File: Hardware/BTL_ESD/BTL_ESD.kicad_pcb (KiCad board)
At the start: 2 copper layers, 73.4 x 95.8 mm, 145 parts, among them J1 DC-005-5A-2.0, J2 BOOT, J3 Load Program, J4 Socket_TFT_1, J5 Socket_TFT_2, J6 USB_B_Micro, J7 220VAC, K1 SRD-05VDC-SL-C, Q1 MMBT2222A, Q2 MMBT2222A, Q3 MMBT2222A, Q4 MMBT2222A, SW1 MS-22D18G2ROHS, SW2 RESET, SW3 ENABLE, SW4 FLASH, U1 ICL7662CBA-T, U2 AMS1117-3.3, U3 TPS54331D, U4 STM32F103RCTx, U5 ESP32-WROOM-32E__4MB_HIGH_TEM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, U6 MCP6002-E_SN, U7 INA128UA, U8 CH340C, U9 PC817, Y1 8MHz, Y2 32.768KHz

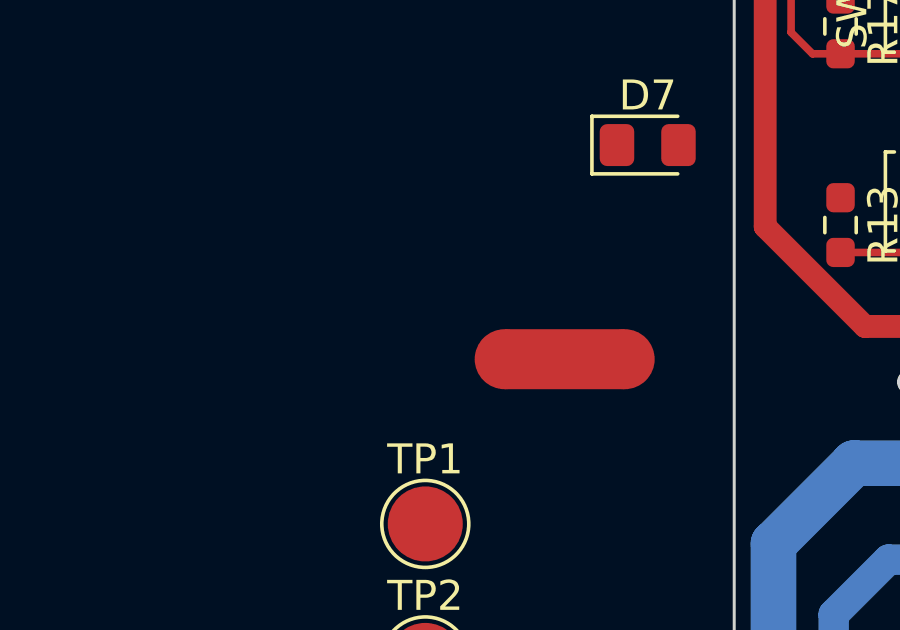
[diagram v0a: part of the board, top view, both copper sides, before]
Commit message: fix:STM32: update structure folder Libs
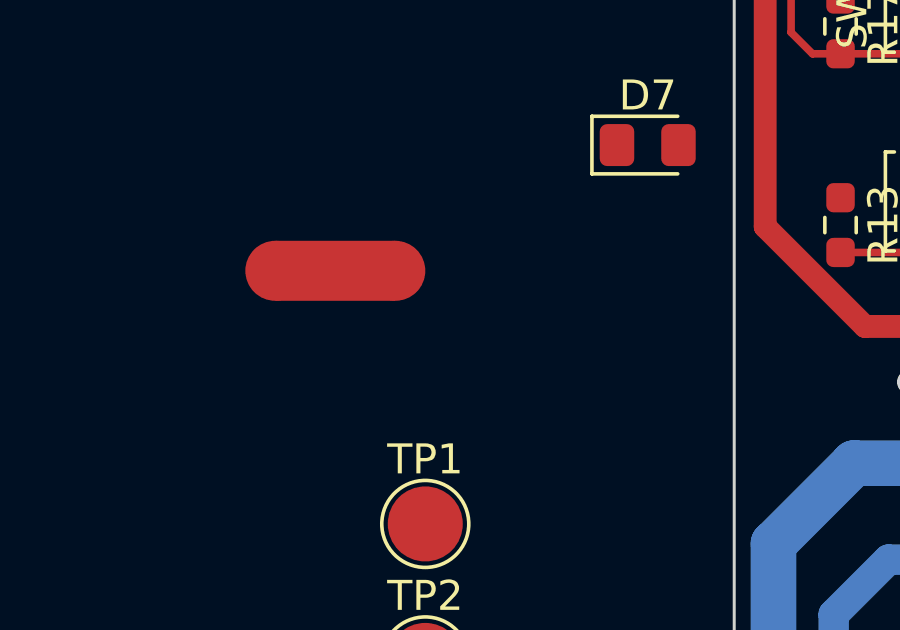
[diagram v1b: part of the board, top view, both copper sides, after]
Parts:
- moved NT1 8.19 mm to (140.0, 88.5)
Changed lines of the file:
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@@
   )
   (footprint "NetTie:NetTie-2_SMD_Pad2.0mm" (layer "F.Cu")
-    (at 147.6248 91.4146)
+    (at 139.9794 88.4682)
     (descr "Net tie, 2 pin, 2.0mm square SMD pads")
     (tags "net tie")

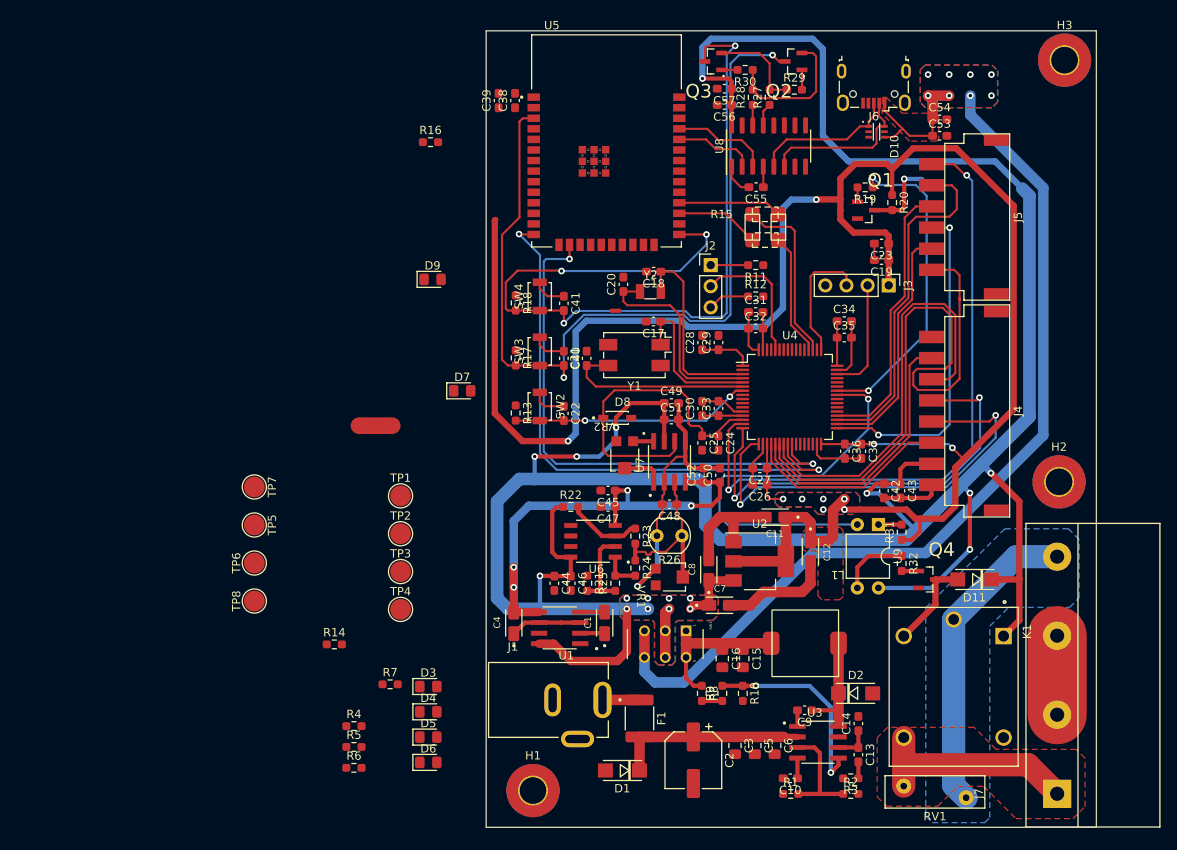
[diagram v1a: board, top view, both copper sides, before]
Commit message: hardware:update pcb track power
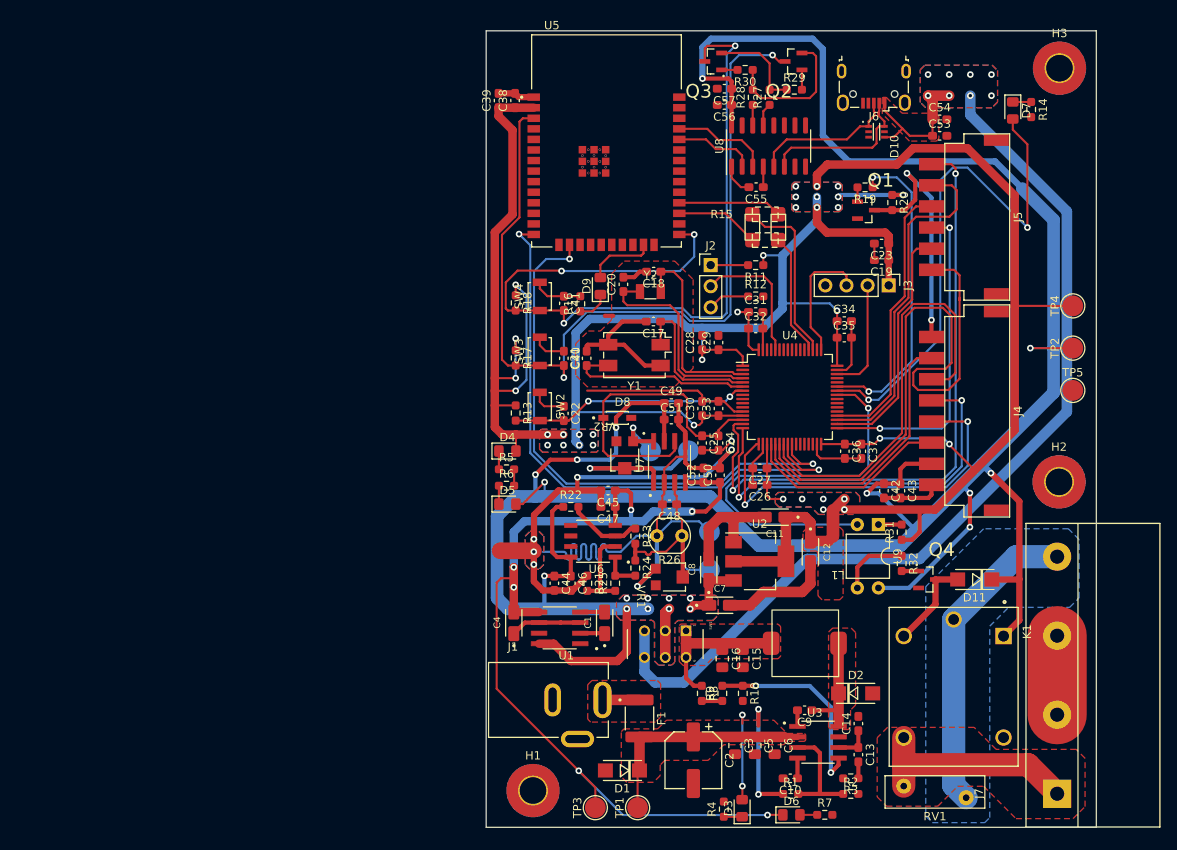
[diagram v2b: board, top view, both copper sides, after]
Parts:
- added TP5: GND, TestPoint:TestPoint_Pad_D2.5mm, F.Cu at (223.8, 84.2)
- TP6: renamed from TP5; moved to B.Cu
- TP7: renamed from TP6; moved to B.Cu
- TP8: renamed from TP7; moved to B.Cu
- TP9: renamed from TP8; moved to B.Cu
- moved R14 105.6 mm to (218.8, 50.5), turned to -90 degrees
- moved TP4 88.7 mm to (223.8, 74.1), turned to 90 degrees
- moved TP2 83.8 mm to (223.8, 79.1), turned to 90 degrees
- moved D7 74.3 mm to (216.6, 50.6), turned to -90 degrees
- moved TP6 55.0 mm to (180.1, 105.8), turned to 90 degrees
- moved TP7 54.8 mm to (180.1, 101.2)
- moved R7 54.6 mm to (194.0, 135.3)
- moved TP8 52.4 mm to (177.6, 91.5), turned to 180 degrees
- moved TP9 50.9 mm to (173.0, 91.5), turned to 180 degrees
- moved TP1 47.1 mm to (171.5, 134.4), turned to 90 degrees
- moved R4 45.6 mm to (181.8, 134.6), turned to 90 degrees
- moved D6 44.1 mm to (190.0, 135.3)
- moved D3 40.5 mm to (184.0, 134.5), turned to 90 degrees
- moved R6 38.6 mm to (155.7, 95.7)
- moved R5 38.1 mm to (155.7, 93.7)
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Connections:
- R13 pad 1: +3.3V -> +3V3
- U4 pad 2: /STM32/LED_TEST -> unconnected-(U4-PC13-Pad2)
- U4 pad 42: TFT_BL -> /STM32/LED_TEST
- U4 pad 43: unconnected-(U4-PA10-Pad43) -> TFT_BL
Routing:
- net +3V3: track 270.4 -> 370.1 mm, vias 10 -> 35
- net GNDA: track 33.6 -> 122.3 mm, vias 1 -> 6
- net /STM32/LED_TEST: track 0.00 -> 62.8 mm, vias 0 -> 2
- net -5V: track 55.9 -> 118.1 mm, vias 4 -> 6
- net VCC: track 23.0 -> 54.1 mm, vias 0 -> 4
- net GND: track 90.4 -> 117.6 mm, vias 0 -> 1
- net GND1: track 0.00 -> 20.0 mm
- net /TFT/CONTROL_BL: track 10.9 -> 29.9 mm, vias 1 -> 2
- net Net-(TP8-Pad1): track 4.97 -> 21.9 mm, vias 0 -> 1
- net +5V: track 343.5 -> 354.8 mm, vias 17 -> 19
- net /ESP32/LED_STATUS: track 0.00 -> 8.29 mm
- net CURRENT_SUPPLY: track 20.6 -> 27.5 mm
- net TFT_RESET: track 53.5 -> 46.5 mm
- net Net-(TP9-Pad1): track 2.47 -> 7.72 mm, vias 0 -> 1
- net TFT_DC_RS: track 52.8 -> 48.4 mm
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- added copper zone on F.Cu, net GND1
- added copper zone on B.Cu, net GNDA
- added copper zone on F.Cu, net GNDA
- added copper zone on F.Cu, net Net-(F1-Pad1)
- added copper zone on F.Cu, net Net-(U3-PH)
- added copper zone on F.Cu, net VCC
- added copper zone on F.Cu, net Vin

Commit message: update
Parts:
- Q2, Q3, R27, R28, R29, R30: moved to B.Cu
- moved Q3 15.2 mm to (184.5, 59.3), turned to -90 degrees
- moved Q2 11.7 mm to (182.2, 53.2)
- moved R30 10.5 mm to (184.4, 56.2)
- moved R29 8.41 mm to (188.2, 56.2)
- moved C40 6.61 mm to (162.6, 73.8)
- moved C41 6.61 mm to (162.6, 80.4)
- moved R17 6.61 mm to (156.8, 73.7)
- moved R18 6.61 mm to (156.8, 80.3)
- moved SW3 6.61 mm to (159.7, 72.9)
- moved SW4 6.61 mm to (159.7, 79.5)
- moved R27 4.32 mm to (187.2, 53.3), turned to -90 degrees
- moved R28 4.32 mm to (185.3, 53.3), turned to -90 degrees
- moved C57 2.59 mm to (183.5, 50.0), turned to 0 degrees
- moved H3 2.44 mm to (222.3, 47.9)
- moved C56 2.28 mm to (179.6, 50.0)
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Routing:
- net EN: track 105.1 -> 78.7 mm, vias 2 -> 3
- net +5V: track 354.8 -> 336.2 mm
- net Net-(Q2-Pad1): track 2.38 -> 16.8 mm
- net RTS: track 16.9 -> 4.07 mm
- net FLASH: track 99.1 -> 89.6 mm, vias 4 -> 3
- net GND: track 117.6 -> 124.3 mm, vias 1 -> 88
- net DIR: track 11.5 -> 5.53 mm
- net GNDA: track 122.3 -> 116.8 mm, vias 6 -> 5
- net V_USB: track 130.6 -> 133.6 mm, vias 8 -> 6
- net +3V3: track 370.1 -> 367.4 mm
- net Net-(U8-~{RTS}): track 2.47 -> 4.75 mm, vias 0 -> 1
- net /STM32/LED_TEST: track 62.8 -> 64.6 mm
- net Net-(U8-~{DTR}): track 2.79 -> 4.56 mm, vias 0 -> 1
- net GND1: track 20.0 -> 21.4 mm
- net /STM32/SWCLK: track 15.2 -> 16.0 mm
- added copper zone on B.Cu, net GND
- added copper zone on F.Cu, net GND
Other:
- board size 73.4 x 95.8 mm -> 73.5 x 92.9 mm

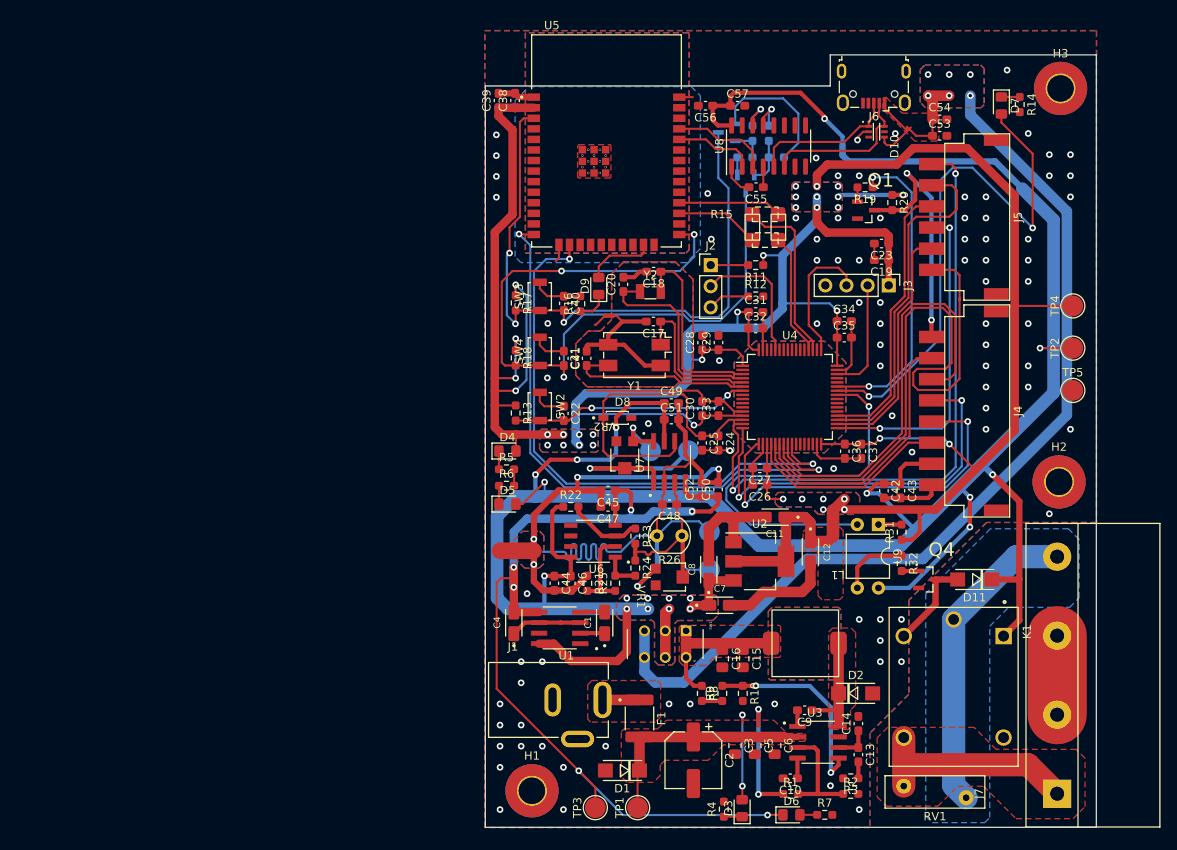
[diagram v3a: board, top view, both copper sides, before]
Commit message: file:STM32: update structure folder
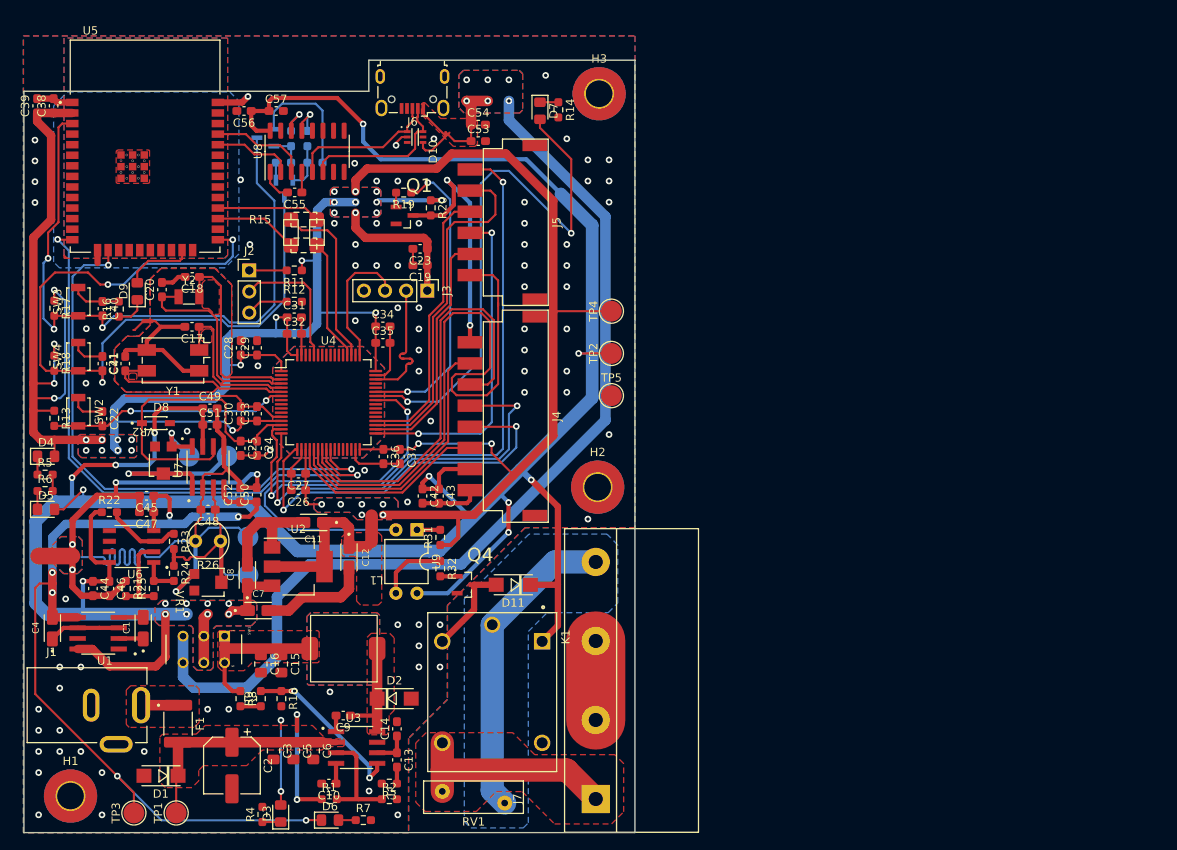
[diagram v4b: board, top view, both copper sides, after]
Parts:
- moved C21 55.5 mm to (109.9, 81.0)
- moved C50 55.5 mm to (125.7, 96.8)
- moved C52 55.5 mm to (123.7, 96.8)
- moved R16 55.5 mm to (109.1, 74.4)
- moved R4 55.5 mm to (126.4, 135.2)
- moved U6 55.5 mm to (110.6, 103.0)
- moved C10 55.5 mm to (134.4, 131.5)
- moved C11 55.5 mm to (132.5, 100.1)
- moved C12 55.5 mm to (136.8, 104.3)
- moved C13 55.5 mm to (142.5, 128.7)
- moved C14 55.5 mm to (142.5, 124.9)
- moved C17 55.5 mm to (117.9, 76.6)
- moved C18 55.5 mm to (117.9, 70.6)
- moved C19 55.5 mm to (145.3, 69.2)
- moved C2 55.5 mm to (122.7, 129.3)
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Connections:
- U5 pad 39_10: (no net) -> GND
- U5 pad 39_11: (no net) -> GND
- U5 pad 39_12: (no net) -> GND
- U5 pad 39_13: (no net) -> GND
- U5 pad 39_14: (no net) -> GND
- U5 pad 39_15: (no net) -> GND
- U5 pad 39_16: (no net) -> GND
- U5 pad 39_17: (no net) -> GND
- U5 pad 39_18: (no net) -> GND
- U5 pad 39_19: (no net) -> GND
- U5 pad 39_20: (no net) -> GND
- U5 pad 39_21: (no net) -> GND
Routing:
- net V_USB: track 133.6 -> 137.8 mm
- net Net-(U3-VSENSE): track 24.1 -> 20.3 mm
- net /STM32/SWDIO: track 13.7 -> 16.0 mm
- net GND: track 124.3 -> 126.5 mm, vias 88 -> 83
- net TFT_DC_RS: track 48.4 -> 50.3 mm
- net Net-(Q2-Pad1): track 16.8 -> 15.0 mm
- net +3V3: track 367.4 -> 369.2 mm
- net /STM32/LED_TEST: track 64.6 -> 66.0 mm
- net CONTROL_LED: track 48.3 -> 47.0 mm
- net EN: track 78.7 -> 79.6 mm
- net TFT_BL: track 37.2 -> 36.3 mm
- net +5V: track 336.2 -> 335.4 mm
- net TFT_RESET: track 46.5 -> 47.4 mm
- net GNDA: track 116.8 -> 116.1 mm
- net SPI2_CS: track 39.3 -> 39.9 mm
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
